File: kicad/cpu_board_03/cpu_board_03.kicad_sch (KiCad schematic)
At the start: 62 parts, among them J1 DIN41612_02x32_AC, J11 Conn_01x09, J2 Clock, J6 Conn_01x02_Socket, J9 Ram1 Enable, SW1 SW_Reset, SW2 SW_PWR, U1 W65C02SxP, U10 74HC245, U13 74AHC1G32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

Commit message: updated routing & semi-final checks
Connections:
- net GND: now also J1.c20 (Pin_c20)
- net VCC: now also J1.a20 (Pin_a20)
- no-connect marks 14 -> 25
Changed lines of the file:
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@@
+	)
+	(junction
+		(at 339.09 213.36)
+		(diameter 0)
+		(color 0 0 0 0)
 	)
 	(junction
@@
 	)
 	(junction
+		(at 368.3 213.36)
+		(diameter 0)
+		(color 0 0 0 0)
+	)
+	(junction
 		(at 264.16 265.43)
 		(diameter 0)
@@
 	)
 	(no_connect
+		(at 349.25 228.6)
+	)
+	(no_connect
+		(at 361.95 228.6)
+	)
+	(no_connect
 		(at 361.95 220.98)
 	)
@@
 	)
 	(no_connect
+		(at 349.25 233.68)
+	)
+	(no_connect
 		(at 349.25 223.52)
+	)
+	(no_connect
+		(at 361.95 226.06)
+	)
+	(no_connect
+		(at 349.25 238.76)
 	)
 	(no_connect
@@
 	)
 	(no_connect
+		(at 361.95 238.76)
+	)
+	(no_connect
+		(at 361.95 231.14)
+	)
+	(no_connect
 		(at 54.61 66.04)
 	)
@@
 	)
 	(no_connect
+		(at 349.25 231.14)
+	)
+	(no_connect
 		(at 36.83 157.48)
+	)
+	(no_connect
+		(at 361.95 233.68)
 	)
 	(no_connect
@@
 		(at 142.24 33.02)
 	)
+	(no_connect
+		(at 361.95 236.22)
+	)
+	(no_connect
+		(at 349.25 236.22)
+	)
 	(wire
 		(pts
@@
 	(wire
 		(pts
+			(xy 339.09 213.36) (xy 349.25 213.36)
+		)
+		(stroke
+			(width 0)
+			(type default)
+		)
+	)
+	(wire
+		(pts
 			(xy 260.35 182.88) (xy 270.51 182.88)
 		)
@@
 	(wire
 		(pts
-			(xy 339.09 200.66) (xy 339.09 243.84)
+			(xy 339.09 200.66) (xy 339.09 213.36)
 		)
 		(stroke
@@
 	(wire
 		(pts
+			(xy 361.95 213.36) (xy 368.3 213.36)
+		)
+		(stroke
+			(width 0)
+			(type default)
+		)
+	)
+	(wire
+		(pts
 			(xy 271.78 148.59) (xy 271.78 147.32)
 		)
@@
 	(wire
 		(pts
+			(xy 339.09 213.36) (xy 339.09 243.84)
+		)
+		(stroke
+			(width 0)
+			(type default)
+		)
+	)
+	(wire
+		(pts
 			(xy 233.68 185.42) (xy 234.95 185.42)
 		)
@@
 	(wire
 		(pts
+			(xy 368.3 213.36) (xy 368.3 243.84)
+		)
+		(stroke
+			(width 0)
+			(type default)
+		)
+	)
+	(wire
+		(pts
 			(xy 62.23 243.84) (xy 60.96 243.84)
 		)
@@
 	(wire
 		(pts
-			(xy 368.3 200.66) (xy 368.3 243.84)
-		)
-		(stroke
+			(xy 368.3 200.66) (xy 368.3 213.36)
+		)
+		(stroke

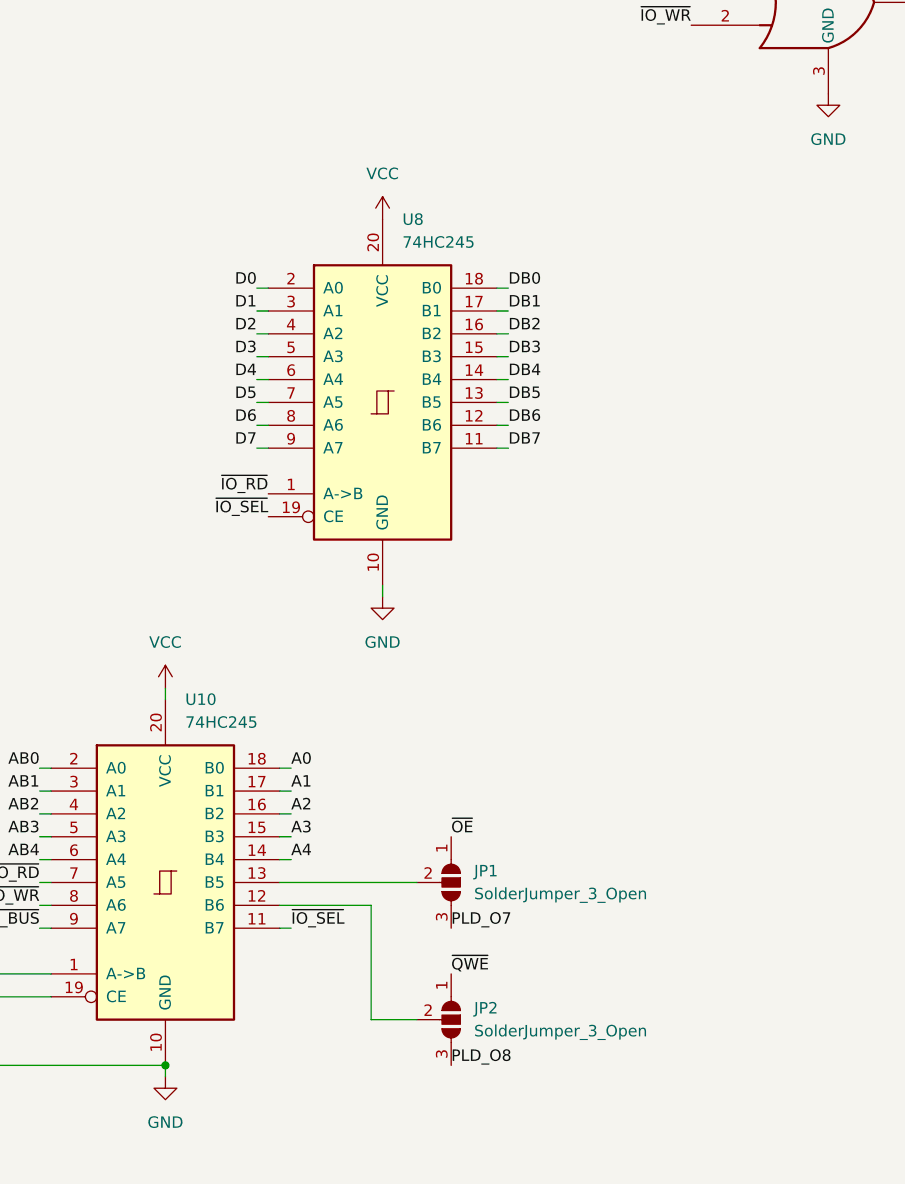
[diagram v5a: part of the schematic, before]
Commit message: uodate bus ow/wr signals
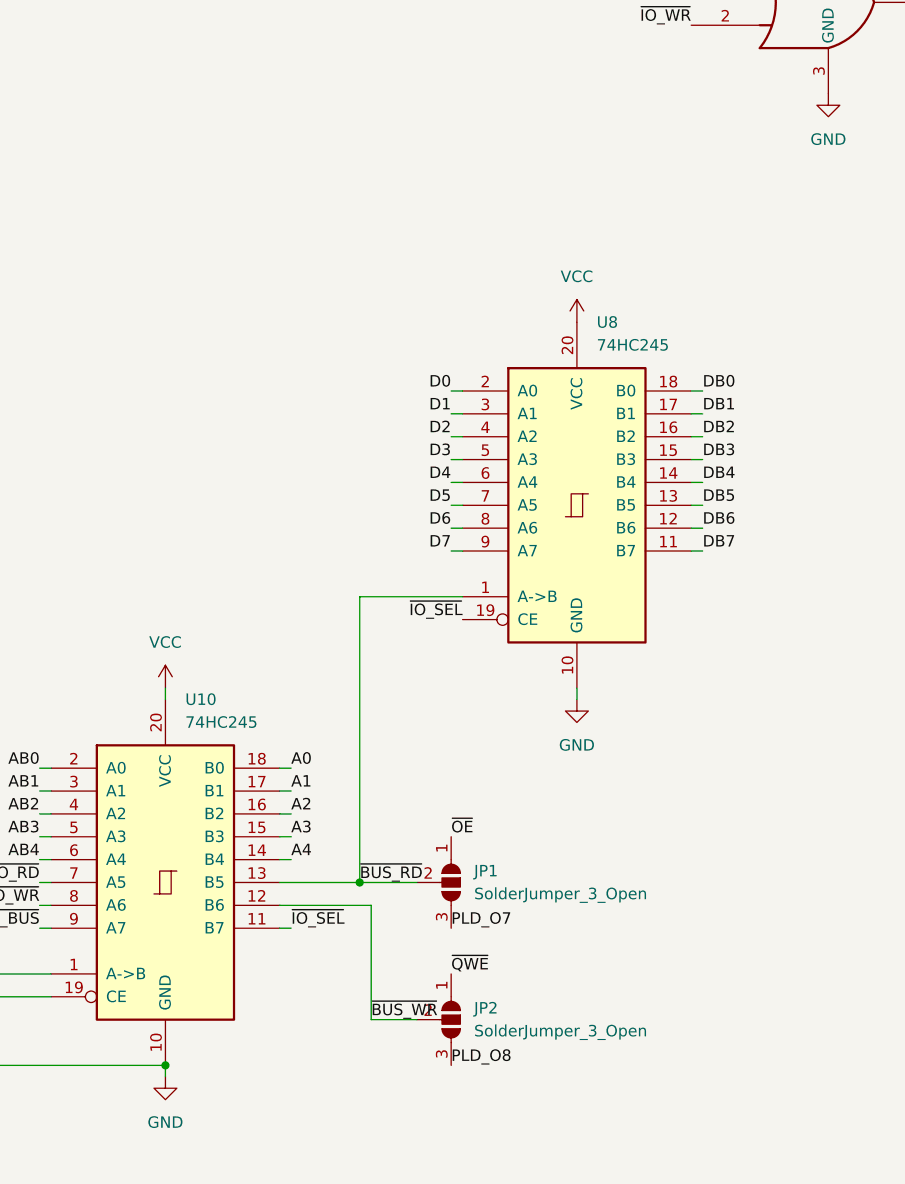
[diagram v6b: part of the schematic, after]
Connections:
- net ~{IO_RD}: no longer U8.1 (A->B)
- net ~{BUS_WR}: now reaches JP2.2 (C), U10.12 (B6)
- net ~{BUS_RD}: now reaches JP1.2 (C), U10.13 (B5)
- net ~{BUS_RD}: now also U8.1 (A->B)
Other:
- moved on the sheet: U8
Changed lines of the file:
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@@
 	)
 	(junction
+		(at 269.24 180.34)
+		(diameter 0)
+		(color 0 0 0 0)
+	)
+	(junction
 		(at 295.91 41.91)
 		(diameter 0)
@@
 	(wire
 		(pts
+			(xy 269.24 180.34) (xy 275.59 180.34)
+		)
+		(stroke
+			(width 0)
+			(type default)
+		)
+	)
+	(wire
+		(pts
 			(xy 180.34 167.64) (xy 181.61 167.64)
 		)
@@
 	(wire
 		(pts
-			(xy 285.75 116.84) (xy 284.48 116.84)
+			(xy 307.34 128.27) (xy 306.07 128.27)
 		)
 		(stroke
@@
 	(wire
 		(pts
-			(xy 285.75 132.08) (xy 284.48 132.08)
+			(xy 307.34 143.51) (xy 306.07 143.51)
 		)
 		(stroke
@@
 	(wire
 		(pts
+			(xy 269.24 148.59) (xy 280.67 148.59)
+		)
+		(stroke
+			(width 0)
+			(type default)
+		)
+	)
+	(wire
+		(pts
 			(xy 261.62 238.76) (xy 261.62 241.3)
 		)
@@
 	(wire
 		(pts
-			(xy 285.75 124.46) (xy 284.48 124.46)
+			(xy 307.34 135.89) (xy 306.07 135.89)
 		)
 		(stroke
@@
 	(wire
 		(pts
-			(xy 285.75 121.92) (xy 284.48 121.92)
+			(xy 307.34 133.35) (xy 306.07 133.35)
 		)
 		(stroke
@@
 	(wire
 		(pts
-			(xy 257.81 114.3) (xy 259.08 114.3)
+			(xy 279.4 125.73) (xy 280.67 125.73)
 		)
 		(stroke
@@
 	(wire
 		(pts
-			(xy 271.78 148.59) (xy 271.78 147.32)
+			(xy 293.37 160.02) (xy 293.37 158.75)
 		)
 		(stroke
@@
 	(wire
 		(pts
-			(xy 257.81 132.08) (xy 259.08 132.08)
+			(xy 279.4 143.51) (xy 280.67 143.51)
 		)
 		(stroke
@@
 	(wire
 		(pts
-			(xy 257.81 121.92) (xy 259.08 121.92)
+			(xy 279.4 133.35) (xy 280.67 133.35)
 		)
 		(stroke
@@
 	(wire
 		(pts
-			(xy 257.81 119.38) (xy 259.08 119.38)
+			(xy 279.4 130.81) (xy 280.67 130.81)
 		)
 		(stroke
@@
 	(wire
 		(pts
-			(xy 257.81 116.84) (xy 259.08 116.84)
+			(xy 279.4 128.27) (xy 280.67 128.27)
 		)
 		(stroke
@@
 	(wire
 		(pts
-			(xy 285.75 129.54) (xy 284.48 129.54)
+			(xy 307.34 140.97) (xy 306.07 140.97)
 		)
 		(stroke
@@
 	(wire
 		(pts
-			(xy 285.75 127) (xy 284.48 127)
+			(xy 307.34 138.43) (xy 306.07 138.43)
 		)
 		(stroke
@@
 	(wire
 		(pts
-			(xy 257.81 124.46) (xy 259.08 124.46)
+			(xy 279.4 135.89) (xy 280.67 135.89)
 		)
 		(stroke
@@
 	(wire
 		(pts
+			(xy 269.24 180.34) (xy 269.24 148.59)
+		)
+		(stroke
+			(width 0)
+			(type default)
+		)
+	)
+	(wire
+		(pts
 			(xy 180.34 154.94) (xy 181.61 154.94)
 		)
@@
 	(wire
 		(pts
-			(xy 285.75 114.3) (xy 284.48 114.3)
+			(xy 307.34 125.73) (xy 306.07 125.73)
 		)
 		(stroke
@@
 	(wire
 		(pts
-			(xy 260.35 180.34) (xy 275.59 180.34)
+			(xy 260.35 180.34) (xy 269.24 180.34)
 		)
 		(stroke
@@
 	(wire
 		(pts
-			(xy 257.81 129.54) (xy 259.08 129.54)
+			(xy 279.4 140.97) (xy 280.67 140.97)
 		)
 		(stroke
@@
 	(wire
 		(pts
-			(xy 257.81 127) (xy 259.08 127)
+			(xy 279.4 138.43) (xy 280.67 138.43)
 		)
 		(stroke
@@
 	(wire
 		(pts
-			(xy 285.75 119.38) (xy 284.48 119.38)
+			(xy 307.34 130.81) (xy 306.07 130.81)
 		)
 		(stroke
@@
 	)
 	(label "DB6"
-		(at 285.75 129.54 0)
+		(at 307.34 140.97 0)
 		(effects
 			(font
@@
 	)
 	(label "D0"
-		(at 257.81 114.3 180)
+		(at 279.4 125.73 180)
 		(effects
 			(font
@@
 	)
 	(label "D7"
-		(at 257.81 132.08 180)
+		(at 279.4 143.51 180)
 		(effects
 			(font
@@
 	)
 	(label "DB4"
-		(at 285.75 124.46 0)
+		(at 307.34 135.89 0)
 		(effects
 			(font
@@
 		)
 	)
-	(label "~{IO_RD}"
-		(at 259.08 137.16 180)
-		(effects
-			(font
-				(size 1.27 1.27)
-			)
-			(justify right bottom)
-		)
-	)
 	(label "DB4"
 		(at 349.25 170.18 180)
@@
 	)
 	(label "DB7"
-		(at 285.75 132.08 0)
+		(at 307.34 143.51 0)
 		(effects
 			(font
@@
 	)
 	(label "D4"
-		(at 257.81 124.46 180)
+		(at 279.4 135.89 180)
 		(effects
 			(font
@@
 	)
 	(label "~{IO_SEL}"
-		(at 259.08 139.7 180)
+		(at 280.67 151.13 180)
 		(effects
 			(font
@@
 	)
 	(label "D3"
-		(at 257.81 121.92 180)
+		(at 279.4 133.35 180)
 		(effects
 			(font
@@
 	)
 	(label "DB5"
-		(at 285.75 127 0)
+		(at 307.34 138.43 0)
 		(effects
 			(font
@@
 	)
 	(label "D1"
-		(at 257.81 116.84 180)
+		(at 279.4 128.27 180)
 		(effects
 			(font
@@
 	)
 	(label "DB2"
-		(at 285.75 119.38 0)
+		(at 307.34 130.81 0)
 		(effects
 			(font
@@
 	)
 	(label "DB1"
-		(at 285.75 116.84 0)
+		(at 307.34 128.27 0)
 		(effects
 			(font
@@
 	)
 	(label "DB3"
-		(at 285.75 121.92 0)
+		(at 307.34 133.35 0)
 		(effects
 			(font
@@
 	)
 	(label "DB0"
-		(at 285.75 114.3 0)
+		(at 307.34 125.73 0)
 		(effects
 			(font
@@
 	)
 	(label "D6"
-		(at 257.81 129.54 180)
+		(at 279.4 140.97 180)
 		(effects
 			(font
@@
 	)
 	(label "D2"
-		(at 257.81 119.38 180)
+		(at 279.4 130.81 180)
 		(effects
 			(font
@@
 		)
 	)
+	(label "~{BUS_WR}"
+		(at 270.51 195.58 0)
+		(effects
+			(font
+				(size 1.27 1.27)
+			)
+			(justify left bottom)
+		)
+	)
 	(label "D2"
 		(at 58.42 165.1 0)
@@
 	)
 	(label "D5"
-		(at 257.81 127 180)
+		(at 279.4 138.43 180)
 		(effects
 			(font
@@
 		)
 	)
+	(label "~{BUS_RD}"
+		(at 269.24 180.34 0)
+		(effects
+			(font
+				(size 1.27 1.27)
+			)
+			(justify left bottom)
+		)
+	)
 	(label "PLD_O7"
 		(at 361.95 182.88 0)
@@
 	(symbol
 		(lib_id "power:GND")
-		(at 271.78 148.59 0)
+		(at 293.37 160.02 0)
 		(unit 1)
 		(exclude_from_sim no)
@@
 		(fields_autoplaced yes)
 		(property "Reference" "#PWR028"
-			(at 271.78 154.94 0)
+			(at 293.37 166.37 0)
 			(effects
 				(font
@@
 		)
 		(property "Value" "GND"
-			(at 271.78 153.67 0)
+			(at 293.37 165.1 0)
 			(effects
 				(font
@@
 		)
 		(property "Footprint" ""
-			(at 271.78 148.59 0)
+			(at 293.37 160.02 0)
 			(effects
 				(font
@@
 		)
 		(property "Datasheet" ""
-			(at 271.78 148.59 0)
+			(at 293.37 160.02 0)
 			(effects
 				(font
@@
 		)
 		(property "Description" ""
-			(at 271.78 148.59 0)
+			(at 293.37 160.02 0)
 			(effects
 				(font
@@
 	(symbol
 		(lib_id "74xx:74HC245")
-		(at 271.78 127 0)
+		(at 293.37 138.43 0)
 		(unit 1)
 		(exclude_from_sim no)
@@
 		(fields_autoplaced yes)
 		(property "Reference" "U8"
-			(at 273.9741 106.68 0)
+			(at 295.5641 118.11 0)
 			(effects
 				(font
@@
 		)
 		(property "Value" "74HC245"
-			(at 273.9741 109.22 0)
+			(at 295.5641 120.65 0)
 			(effects
 				(font
@@
 		)
 		(property "Footprint" "Package_SO:SO-20_12.8x7.5mm_P1.27mm"
-			(at 271.78 127 0)
+			(at 293.37 138.43 0)
 			(effects
 				(font
@@
 		)
 		(property "Datasheet" "http://www.ti.com/lit/gpn/sn74HC245"
-			(at 271.78 127 0)
+			(at 293.37 138.43 0)
 			(effects
 				(font
@@
 		)
 		(property "Description" ""
-			(at 271.78 127 0)
+			(at 293.37 138.43 0)
 			(effects
 				(font
@@
 	(symbol
 		(lib_id "power:VCC")
-		(at 271.78 106.68 0)
+		(at 293.37 118.11 0)
 		(unit 1)
 		(exclude_from_sim no)
@@
 		(fields_autoplaced yes)
 		(property "Reference" "#PWR015"
-			(at 271.78 110.49 0)
+			(at 293.37 121.92 0)
 			(effects
 				(font
@@
 		)
 		(property "Value" "VCC"
-			(at 271.78 101.6 0)
+			(at 293.37 113.03 0)
 			(effects
 				(font
@@
 		)
 		(property "Footprint" ""
-			(at 271.78 106.68 0)
+			(at 293.37 118.11 0)
 			(effects
 				(font
@@
 		)
 		(property "Datasheet" ""
-			(at 271.78 106.68 0)
+			(at 293.37 118.11 0)
 			(effects
 				(font
@@
 		)
 		(property "Description" ""
-			(at 271.78 106.68 0)
+			(at 293.37 118.11 0)
 			(effects
 				(font

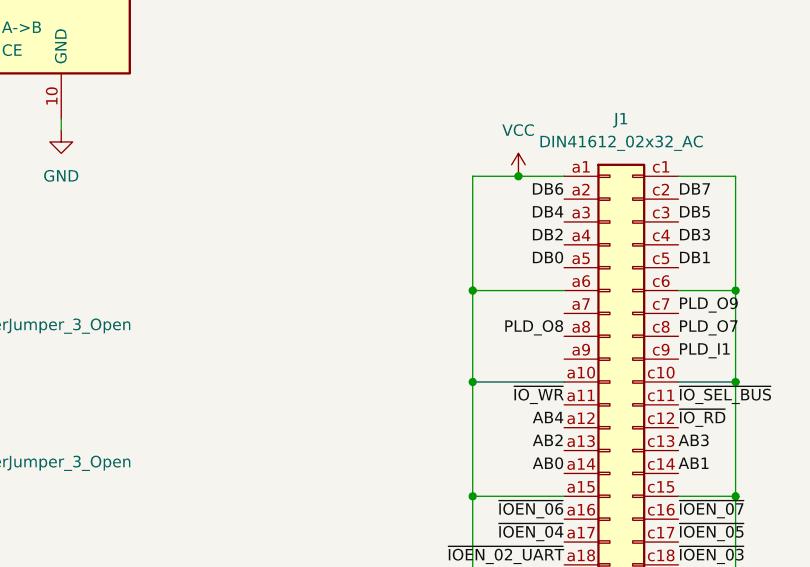
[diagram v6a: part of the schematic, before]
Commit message: optimize routing / grounding
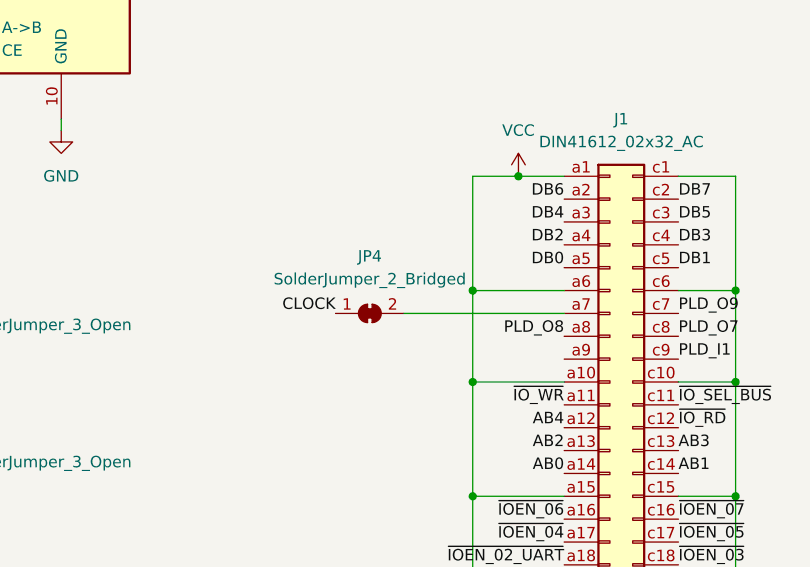
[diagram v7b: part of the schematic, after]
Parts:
- added JP4: SolderJumper_2_Bridged, Jumper:SolderJumper-2_P1.3mm_Bridged_RoundedPad1.0x1.5mm, symbol Jumper:SolderJumper_2_Bridged
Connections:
- net CLOCK: now also JP4.1 (A)
- net at J1.a7 (Pin_a7): now also JP4.2 (B)
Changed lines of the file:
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@@
 	(wire
 		(pts
+			(xy 331.47 180.34) (xy 349.25 180.34)
+		)
+		(stroke
+			(width 0)
+			(type default)
+		)
+	)
+	(wire
+		(pts
 			(xy 58.42 121.92) (xy 57.15 121.92)
 		)
@@
 		)
 	)
+	(label "CLOCK"
+		(at 323.85 180.34 180)
+		(effects
+			(font
+				(size 1.27 1.27)
+			)
+			(justify right bottom)
+		)
+	)
 	(label "~{OE}"
 		(at 180.34 175.26 180)
@@
 					(unit 1)
 				)
+			)
+		)
+	)
+	(symbol
+		(lib_id "Jumper:SolderJumper_2_Bridged")
+		(at 327.66 180.34 0)
+		(unit 1)
+		(exclude_from_sim no)
+		(in_bom yes)
+		(on_board yes)
+		(dnp no)
+		(fields_autoplaced yes)
+		(property "Reference" "JP4"
+			(at 327.66 173.99 0)
+			(effects
+				(font
+					(size 1.27 1.27)
+				)
+			)
+		)
+		(property "Value" "SolderJumper_2_Bridged"
+			(at 327.66 176.53 0)
+			(effects
+				(font
+					(size 1.27 1.27)
+				)
+			)
+		)
+		(property "Footprint" "Jumper:SolderJumper-2_P1.3mm_Bridged_RoundedPad1.0x1.5mm"
+			(at 327.66 180.34 0)
+			(effects
+				(font
+					(size 1.27 1.27)
+				)
+				(hide yes)
+			)
+		)
+		(property "Datasheet" "~"
+			(at 327.66 180.34 0)
+			(effects
+				(font
+					(size 1.27 1.27)
+				)
+				(hide yes)
+			)
+		)
+		(property "Description" "Solder Jumper, 2-pole, closed/bridged"
+			(at 327.66 180.34 0)
+			(effects
+				(font
+					(size 1.27 1.27)
+				)
+				(hide yes)
+			)
+		)
+		(pin "2"
+		)
+		(pin "1"
+		)
+		(instances
+			(project ""
+				(path "/a9a73dc6-7f92-4458-9da8-49621d12e480"
+					(reference "JP4")
+					(unit 1)
+				)

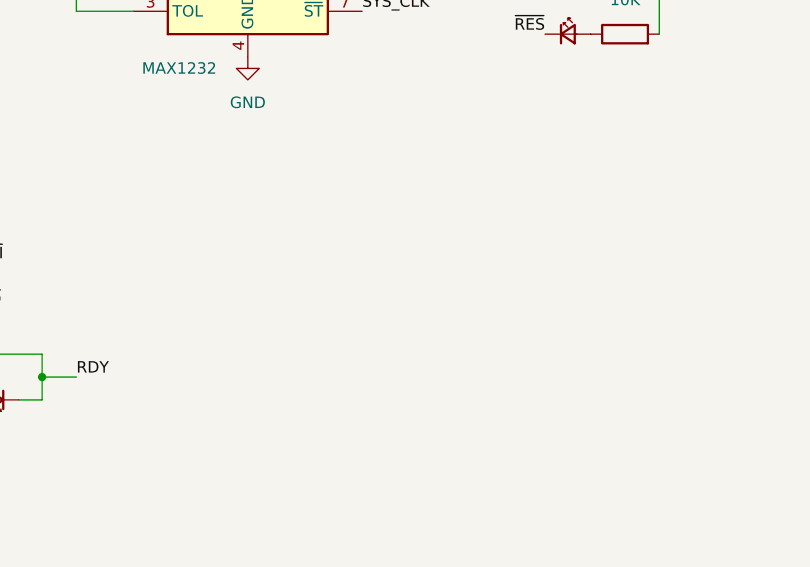
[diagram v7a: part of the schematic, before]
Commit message: add GND testpoints
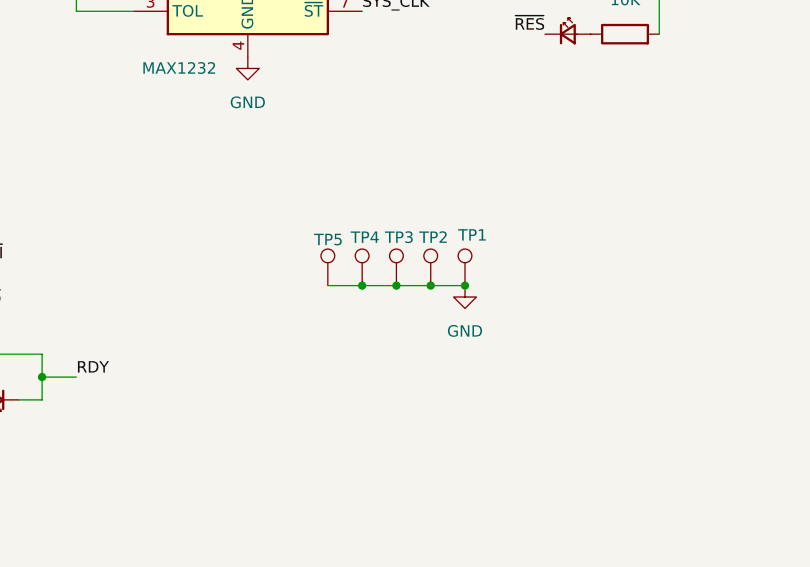
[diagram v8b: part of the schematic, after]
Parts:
- added TP1, TP2, TP3, TP4, TP5: TestPoint, TestPoint:TestPoint_Loop_D1.80mm_Drill1.0mm_Beaded, symbol Connector:TestPoint
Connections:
- net GND: now also TP1.1, TP2.1, TP3.1, TP4.1, TP5.1
